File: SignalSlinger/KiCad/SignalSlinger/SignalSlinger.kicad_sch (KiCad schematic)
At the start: 61 parts, among them J101 Conn_01x02, J102 Conn_01x02, J103 Conn_01x02, J104 Conn_01x02, J105 Conn_01x02, J106 Conn_01x02, J107 DB9 Female, J108 Conn_01x02, J109 Conn_01x03, J110 Conn_01x02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

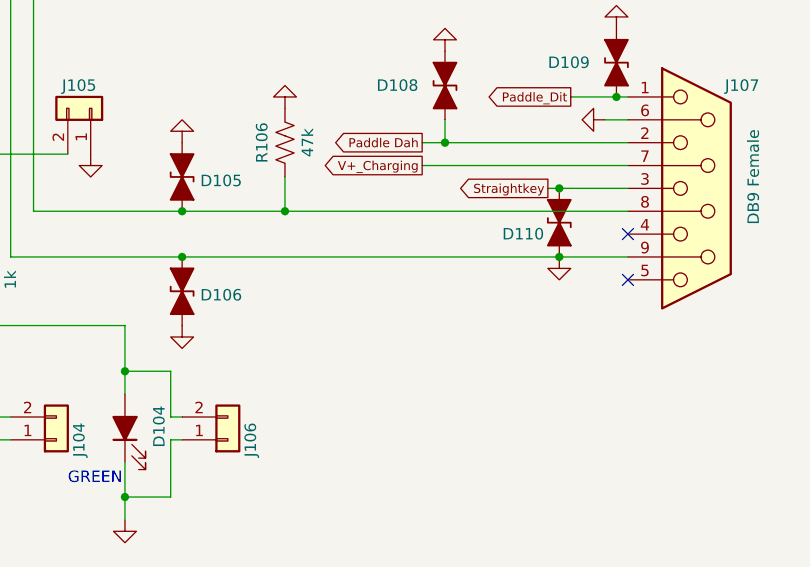
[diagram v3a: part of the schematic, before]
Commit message: Schematic
Corrected another varistor placement error.
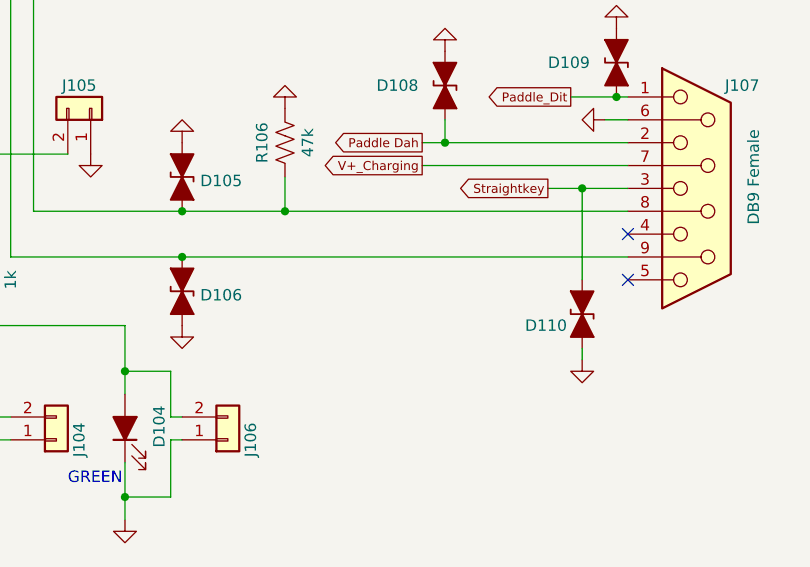
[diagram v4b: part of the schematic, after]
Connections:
- net GND: no longer D106.1 (A1), J107.9, U101.2 (PC0/TxD1)
- new net: D106.1 (A1), J107.9, U101.2 (PC0/TxD1)
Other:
- moved on the sheet: D110
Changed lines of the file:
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@@
     (rev "1.0")
   )
-  (junction (at 158.75 133.35) (diameter 0) (color 0 0 0 0)
-  )
   (junction (at 154.94 81.28) (diameter 0) (color 0 0 0 0)
   )
@@
   (junction (at 120.65 96.52) (diameter 0) (color 0 0 0 0)
   )
-  (junction (at 44.45 146.05) (diameter 0) (color 0 0 0 0)
+  (junction (at 161.29 125.73) (diameter 0) (color 0 0 0 0)
   )
-  (junction (at 158.75 125.73) (diameter 0) (color 0 0 0 0)
+  (junction (at 44.45 146.05) (diameter 0) (color 0 0 0 0)
   )
   (junction (at 101.6 60.96) (diameter 0) (color 0 0 0 0)
@@
     (stroke (width 0) (type default) (color 0 0 0 0))
   )
-  (wire (pts (xy 157.48 125.73) (xy 158.75 125.73))
-    (stroke (width 0) (type default) (color 0 0 0 0))
-  )
   (wire (pts (xy 86.36 160.02) (xy 86.36 157.48))
     (stroke (width 0) (type default) (color 0 0 0 0))
@@
     (stroke (width 0) (type default) (color 0 0 0 0))
   )
+  (wire (pts (xy 161.29 125.73) (xy 161.29 135.89))
+    (stroke (width 0) (type default) (color 0 0 0 0))
+  )
   (wire (pts (xy 49.53 153.67) (xy 53.34 153.67))
     (stroke (width 0) (type default) (color 0 0 0 0))
@@
     (stroke (width 0) (type default) (color 0 0 0 0))
   )
-  (wire (pts (xy 158.75 125.73) (xy 166.37 125.73))
-    (stroke (width 0) (type default) (color 0 0 0 0))
-  )
   (wire (pts (xy 176.53 63.5) (xy 172.72 63.5))
     (stroke (width 0) (type default) (color 0 0 0 0))
@@
     (stroke (width 0) (type default) (color 0 0 0 0))
   )
+  (wire (pts (xy 161.29 143.51) (xy 161.29 144.78))
+    (stroke (width 0) (type default) (color 0 0 0 0))
+  )
   (wire (pts (xy 143.51 120.65) (xy 146.05 120.65))
     (stroke (width 0) (type default) (color 0 0 0 0))
@@
     (stroke (width 0) (type default) (color 0 0 0 0))
   )
-  (wire (pts (xy 116.84 133.35) (xy 158.75 133.35))
-    (stroke (width 0) (type default) (color 0 0 0 0))
-  )
   (wire (pts (xy 101.6 68.58) (xy 101.6 69.85))
     (stroke (width 0) (type default) (color 0 0 0 0))
@@
     (stroke (width 0) (type default) (color 0 0 0 0))
   )
+  (wire (pts (xy 161.29 125.73) (xy 166.37 125.73))
+    (stroke (width 0) (type default) (color 0 0 0 0))
+  )
   (wire (pts (xy 152.4 78.74) (xy 154.94 78.74))
     (stroke (width 0) (type default) (color 0 0 0 0))
@@
     (stroke (width 0) (type default) (color 0 0 0 0))
   )
-  (wire (pts (xy 158.75 133.35) (xy 166.37 133.35))
+  (wire (pts (xy 116.84 133.35) (xy 166.37 133.35))
     (stroke (width 0) (type default) (color 0 0 0 0))
   )
@@
     (stroke (width 0) (type default) (color 0 0 0 0))
   )
+  (wire (pts (xy 157.48 125.73) (xy 161.29 125.73))
+    (stroke (width 0) (type default) (color 0 0 0 0))
+  )
   (wire (pts (xy 255.27 57.15) (xy 255.27 74.93))
     (stroke (width 0) (type default) (color 0 0 0 0))
@@
     (pin "1")
   )
-  (symbol (lib_id "power:GND") (at 158.75 133.35 0) (unit 1)
+  (symbol (lib_id "power:GND") (at 161.29 144.78 0) (unit 1)
     (in_bom yes) (on_board yes) (fields_autoplaced)
-    (property "Reference" "#PWR0158" (id 0) (at 158.75 139.7 0)
+    (property "Reference" "#PWR0158" (id 0) (at 161.29 151.13 0)
       (effects (font (size 1.27 1.27)) hide)
     )
-    (property "Value" "GND" (id 1) (at 158.75 137.7934 0)
+    (property "Value" "GND" (id 1) (at 161.29 149.2234 0)
       (effects (font (size 1.27 1.27)) hide)
     )
-    (property "Footprint" "" (id 2) (at 158.75 133.35 0)
+    (property "Footprint" "" (id 2) (at 161.29 144.78 0)
       (effects (font (size 1.27 1.27)) hide)
     )
-    (property "Datasheet" "" (id 3) (at 158.75 133.35 0)
+    (property "Datasheet" "" (id 3) (at 161.29 144.78 0)
       (effects (font (size 1.27 1.27)) hide)
     )
@@
     (pin "2")
   )
-  (symbol (lib_id "Diode:ESD9B5.0ST5G_1") (at 158.75 129.54 270) (unit 1)
+  (symbol (lib_id "Diode:ESD9B5.0ST5G_1") (at 161.29 139.7 270) (unit 1)
     (in_bom yes) (on_board yes)
-    (property "Reference" "D110" (id 0) (at 152.4 130.81 90)
+    (property "Reference" "D110" (id 0) (at 154.94 140.97 90)
       (effects (font (size 1.27 1.27)) (justify left))
     )
-    (property "Value" "ESD9B5.0ST5G_1" (id 1) (at 157.607 131.5466 90)
+    (property "Value" "ESD9B5.0ST5G_1" (id 1) (at 160.147 141.7066 90)
       (effects (font (size 1.27 1.27)) (justify right) hide)
     )
-    (property "Footprint" "Diode_SMD:D_0603_1608Metric" (id 2) (at 158.75 129.54 0)
+    (property "Footprint" "Diode_SMD:D_0603_1608Metric" (id 2) (at 161.29 139.7 0)
       (effects (font (size 1.27 1.27)) hide)
     )
-    (property "Datasheet" "" (id 3) (at 158.75 129.54 0)
+    (property "Datasheet" "" (id 3) (at 161.29 139.7 0)
       (effects (font (size 1.27 1.27)) hide)
     )
-    (property "Digi-Key Part No." "CG0603MLC-05LECT-ND" (id 4) (at 158.75 129.54 0)
+    (property "Digi-Key Part No." "CG0603MLC-05LECT-ND" (id 4) (at 161.29 139.7 0)
       (effects (font (size 1.27 1.27)) hide)
     )
-    (property "Link" "<a href=\"https://www.digikey.com/products/en?keywords=CG0603MLC-05LECT-ND\">Link</a>" (id 5) (at 158.75 129.54 0)
+    (property "Link" "<a href=\"https://www.digikey.com/products/en?keywords=CG0603MLC-05LECT-ND\">Link</a>" (id 5) (at 161.29 139.7 0)
       (effects (font (size 1.27 1.27)) hide)
     )
-    (property "Manufacturer" "Bourns Inc." (id 6) (at 158.75 129.54 0)
+    (property "Manufacturer" "Bourns Inc." (id 6) (at 161.29 139.7 0)
       (effects (font (size 1.27 1.27)) hide)
     )
-    (property "Manufacturer PN" "CG0603MLC-05LE" (id 7) (at 158.75 129.54 0)
+    (property "Manufacturer PN" "CG0603MLC-05LE" (id 7) (at 161.29 139.7 0)
       (effects (font (size 1.27 1.27)) hide)
     )
-    (property "Description" "VARISTOR 0603" (id 8) (at 158.75 129.54 0)
+    (property "Description" "VARISTOR 0603" (id 8) (at 161.29 139.7 0)
       (effects (font (size 1.27 1.27)) hide)
     )
-    (property "LCSC Part Number" "C316054" (id 9) (at 158.75 129.54 0)
+    (property "LCSC Part Number" "C316054" (id 9) (at 161.29 139.7 0)
       (effects (font (size 1.27 1.27)) hide)
     )

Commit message: PCB Development
First cut at traces
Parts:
- C109: footprint Capacitor_SMD:C_0805_2012Metric_Pad1.18x1.45mm_HandSolder -> Capacitor_SMD:C_0805_2012Metric
- D103: value LED_Filled -> (none); footprint LED_SMD:LED_APDA1806SECK -> (none); Digi-Key Part No. 754-2329-1-ND -> 160-1415-1-ND; Link (none) -> https://www.digikey.com/en/products/detail/liteon/LTST-C170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; Manufacturer Kingbright -> Lite-On Inc.; Manufacturer PN APDA1806SECK/J3-PRV -> LTST-C170KRKT
- D104: value LED_Filled -> (none); footprint LED_SMD:LED_APDA1806SECK -> (none); Digi-Key Part No. 754-2329-1-ND -> 160-1414-1-ND; Link (none) -> https://www.digikey.com/en/products/detail/liteon/LTST-C170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; Manufacturer Kingbright -> Lite-On Inc.; Manufacturer PN APDA1806SECK/J3-PRV -> LTST-C170KGKT
- D107: footprint Package_TO_SOT_SMD:TO-252-3_TabPin2 -> Package_TO_SOT_SMD:TO-252-2
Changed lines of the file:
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@@
     (property "Reference" "C109" (id 0) (at 190.5 38.1 90))
     (property "Value" "10uF" (id 1) (at 189.23 43.18 90))
-    (property "Footprint" "Capacitor_SMD:C_0805_2012Metric_Pad1.18x1.45mm_HandSolder" (id 2) (at 193.04 40.64 0)
+    (property "Footprint" "Capacitor_SMD:C_0805_2012Metric" (id 2) (at 193.04 40.64 0)
       (effects (font (size 1.27 1.27)) hide)
     )
@@
       (effects (font (size 1.27 1.27)) (justify right))
     )
-    (property "Value" "LED_Filled" (id 1) (at 94.361 155.6897 90)
+    (property "Value" "" (id 1) (at 94.361 155.6897 90)
       (effects (font (size 1.27 1.27)) (justify right) hide)
     )
-    (property "Footprint" "LED_SMD:LED_APDA1806SECK" (id 2) (at 91.44 152.4 0)
+    (property "Footprint" "" (id 2) (at 91.44 152.4 0)
       (effects (font (size 1.27 1.27)) hide)
     )
@@
       (effects (font (size 1.27 1.27)) hide)
     )
-    (property "Digi-Key Part No." "754-2329-1-ND" (id 4) (at 91.44 152.4 0)
+    (property "Digi-Key Part No." "160-1415-1-ND" (id 4) (at 91.44 152.4 0)
       (effects (font (size 1.27 1.27)) hide)
     )
-    (property "Manufacturer" "Kingbright" (id 5) (at 91.44 152.4 0)
+    (property "Manufacturer" "Lite-On Inc." (id 5) (at 91.44 152.4 0)
       (effects (font (size 1.27 1.27)) hide)
     )
-    (property "Manufacturer PN" "APDA1806SECK/J3-PRV" (id 6) (at 91.44 152.4 0)
+    (property "Manufacturer PN" "LTST-C170KRKT" (id 6) (at 91.44 152.4 0)
       (effects (font (size 1.27 1.27)) hide)
     )
-    (property "Description" "LED RED CLEAR SMD RIGHT ANGLE" (id 7) (at 91.44 152.4 0)
+    (property "Description" "LED RED CLEAR SMD" (id 7) (at 91.44 152.4 0)
+      (effects (font (size 1.27 1.27)) hide)
+    )
+    (property "Link" "https://www.digikey.com/en/products/detail/liteon/LTST-C170KRKT/386779" (id 8) (at 91.44 152.4 0)
       (effects (font (size 1.27 1.27)) hide)
     )
@@
       (effects (font (size 1.27 1.27)) (justify right))
     )
-    (property "Value" "LED_Filled" (id 1) (at 113.411 155.6897 90)
+    (property "Value" "" (id 1) (at 113.411 155.6897 90)
       (effects (font (size 1.27 1.27)) (justify right) hide)
     )
-    (property "Footprint" "LED_SMD:LED_APDA1806SECK" (id 2) (at 110.49 152.4 0)
+    (property "Footprint" "" (id 2) (at 110.49 152.4 0)
       (effects (font (size 1.27 1.27)) hide)
     )
@@
       (effects (font (size 1.27 1.27)) hide)
     )
-    (property "Digi-Key Part No." "754-2329-1-ND" (id 4) (at 110.49 152.4 0)
+    (property "Digi-Key Part No." "160-1414-1-ND" (id 4) (at 110.49 152.4 0)
+      (effects (font (size 1.27 1.27)) hide)
+    )
+    (property "Manufacturer" "Lite-On Inc." (id 5) (at 110.49 152.4 0)
       (effects (font (size 1.27 1.27)) hide)
     )
-    (property "Manufacturer" "Kingbright" (id 5) (at 110.49 152.4 0)
+    (property "Manufacturer PN" "LTST-C170KGKT" (id 6) (at 110.49 152.4 0)
       (effects (font (size 1.27 1.27)) hide)
     )
-    (property "Manufacturer PN" "APDA1806SECK/J3-PRV" (id 6) (at 110.49 152.4 0)
+    (property "Description" "LED GREEN CLEAR SMD" (id 7) (at 110.49 152.4 0)
       (effects (font (size 1.27 1.27)) hide)
     )
-    (property "Description" "LED RED CLEAR SMD RIGHT ANGLE" (id 7) (at 110.49 152.4 0)
+    (property "Link" "https://www.digikey.com/en/products/detail/liteon/LTST-C170KGKT/386777" (id 8) (at 110.49 152.4 0)
       (effects (font (size 1.27 1.27)) hide)
     )
@@
       (effects (font (size 1.27 1.27)) hide)
     )
+    (property "Description" "CONN HEADER SMD 6POS 2.54MM" (id 8) (at 26.67 101.6 0)
+      (effects (font (size 1.27 1.27)) hide)
+    )
     (pin "1")
     (pin "2")
@@
       (effects (font (size 1.27 1.27)) (justify left))
     )
-    (property "Footprint" "Package_TO_SOT_SMD:TO-252-3_TabPin2" (id 2) (at 196.85 31.75 0)
+    (property "Footprint" "Package_TO_SOT_SMD:TO-252-2" (id 2) (at 196.85 31.75 0)
       (effects (font (size 1.27 1.27)) hide)
     )
@@
     )
     (path "/b7c888bf-e50e-45b8-8886-9bc5abf637fe/09193804-ca67-45ed-822f-cd04d64b6688"
-      (reference "BT201") (unit 1) (value "LiIon Cell") (footprint "Connector_Wire:SolderWire-2.5sqmm_1x02_P7.2mm_D2.4mm_OD3.6mm")
+      (reference "BT201") (unit 1) (value "LiIon Cell") (footprint "Connector_Wire:SolderWire-0.5sqmm_1x02_P4.6mm_D0.9mm_OD2.1mm")
     )
     (path "/5a65e8dc-078c-4a84-92a2-c8664e602338/b9b57d73-b32c-4225-b589-4048e1fc6e82"
@@
     )
     (path "/115b54de-9d4b-4316-864e-ed7acd85bee3"
-      (reference "C109") (unit 1) (value "10uF") (footprint "Capacitor_SMD:C_0805_2012Metric_Pad1.18x1.45mm_HandSolder")
+      (reference "C109") (unit 1) (value "10uF") (footprint "Capacitor_SMD:C_0805_2012Metric")
     )
     (path "/2d9121ff-df85-4a4c-9305-5ac02a8d5857"
@@
     )
     (path "/b7c888bf-e50e-45b8-8886-9bc5abf637fe/5eced5b5-f111-4b62-a0e3-a376cb1cdd4e"
-      (reference "C201") (unit 1) (value "10uF") (footprint "Capacitor_SMD:C_0805_2012Metric_Pad1.18x1.45mm_HandSolder")
+      (reference "C201") (unit 1) (value "10uF") (footprint "Capacitor_SMD:C_0805_2012Metric")
     )
     (path "/b7c888bf-e50e-45b8-8886-9bc5abf637fe/b86b924a-5169-44ab-a9f8-44d35f22ec56"
-      (reference "C202") (unit 1) (value "10nF") (footprint "Capacitor_SMD:C_0805_2012Metric_Pad1.18x1.45mm_HandSolder")
+      (reference "C202") (unit 1) (value "10nF") (footprint "Capacitor_SMD:C_0805_2012Metric")
     )
     (path "/b7c888bf-e50e-45b8-8886-9bc5abf637fe/1021ab69-a748-4b16-a9ce-426860da57fa"
-      (reference "C203") (unit 1) (value "10uF") (footprint "Capacitor_SMD:C_0805_2012Metric_Pad1.18x1.45mm_HandSolder")
+      (reference "C203") (unit 1) (value "10uF") (footprint "Capacitor_SMD:C_0805_2012Metric")
     )
     (path "/b7c888bf-e50e-45b8-8886-9bc5abf637fe/ceb79b4e-7935-40d4-ad84-ef29a96481ff"
@@
     )
     (path "/b7c888bf-e50e-45b8-8886-9bc5abf637fe/3926b98c-997d-4e0b-bdd1-c2b80a8a063e"
-      (reference "C205") (unit 1) (value "10uF") (footprint "Capacitor_SMD:C_0805_2012Metric_Pad1.18x1.45mm_HandSolder")
+      (reference "C205") (unit 1) (value "10uF") (footprint "Capacitor_SMD:C_0805_2012Metric")
     )
     (path "/b7c888bf-e50e-45b8-8886-9bc5abf637fe/22adef07-96a7-4f1f-a966-43837ac6fd49"
-      (reference "C206") (unit 1) (value "10uF") (footprint "Capacitor_SMD:C_0805_2012Metric_Pad1.18x1.45mm_HandSolder")
+      (reference "C206") (unit 1) (value "10uF") (footprint "Capacitor_SMD:C_0805_2012Metric")
     )
     (path "/b7c888bf-e50e-45b8-8886-9bc5abf637fe/cd43bb42-199e-44b1-8ebb-d1bdf511bd6f"
-      (reference "C207") (unit 1) (value "10uF") (footprint "Capacitor_SMD:C_0805_2012Metric_Pad1.18x1.45mm_HandSolder")
+      (reference "C207") (unit 1) (value "10uF") (footprint "Capacitor_SMD:C_0805_2012Metric")
     )
     (path "/b7c888bf-e50e-45b8-8886-9bc5abf637fe/c3586abd-3cdc-46c5-aa0e-93b91497e5f1"
@@
     )
     (path "/b7c888bf-e50e-45b8-8886-9bc5abf637fe/76349d51-f99a-4e96-9064-71be0c436ab8"
-      (reference "C209") (unit 1) (value "10nF") (footprint "Capacitor_SMD:C_0805_2012Metric_Pad1.18x1.45mm_HandSolder")
+      (reference "C209") (unit 1) (value "10nF") (footprint "Capacitor_SMD:C_0805_2012Metric")
     )
     (path "/b7c888bf-e50e-45b8-8886-9bc5abf637fe/77e900cf-5bd6-4c96-af95-a7e4890c98bc"
-      (reference "C210") (unit 1) (value "10uF") (footprint "Capacitor_SMD:C_0805_2012Metric_Pad1.18x1.45mm_HandSolder")
+      (reference "C210") (unit 1) (value "10uF") (footprint "Capacitor_SMD:C_0805_2012Metric")
     )
     (path "/b7c888bf-e50e-45b8-8886-9bc5abf637fe/f751d0b1-e834-4568-8ec6-6c6681f0dd7c"
@@
     )
     (path "/3d96634f-3b26-447f-8ede-f6059a78b14d"
-      (reference "D103") (unit 1) (value "LED_Filled") (footprint "LED_SMD:LED_APDA1806SECK")
+      (reference "D103") (unit 1) (value "Red LED") (footprint "LED_SMD:LED_0805_2012Metric")
     )
     (path "/4be57c09-772e-4b40-9578-77f4049d5694"
-      (reference "D104") (unit 1) (value "LED_Filled") (footprint "LED_SMD:LED_APDA1806SECK")
+      (reference "D104") (unit 1) (value "Green LED") (footprint "LED_SMD:LED_APDA1806SECK")
     )
     (path "/494208f9-e0ca-4027-9207-cba02c8b4cf6"
@@
     )
     (path "/f8ce3bd0-d1d6-4082-8d11-59fe83f61e27"
-      (reference "D107") (unit 1) (value "MBRD10100CT") (footprint "Package_TO_SOT_SMD:TO-252-3_TabPin2")
+      (reference "D107") (unit 1) (value "MBRD10100CT") (footprint "Package_TO_SOT_SMD:TO-252-2")
     )
     (path "/4a4c7e1b-13e6-4f9b-bf07-336fb6deaa8d"
